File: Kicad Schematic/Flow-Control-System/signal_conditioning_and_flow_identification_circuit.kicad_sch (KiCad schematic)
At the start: 22 parts, among them J13 +5V, J14 GND, U6 NE555P, U7 4093, U8 74HC74, U9 4093

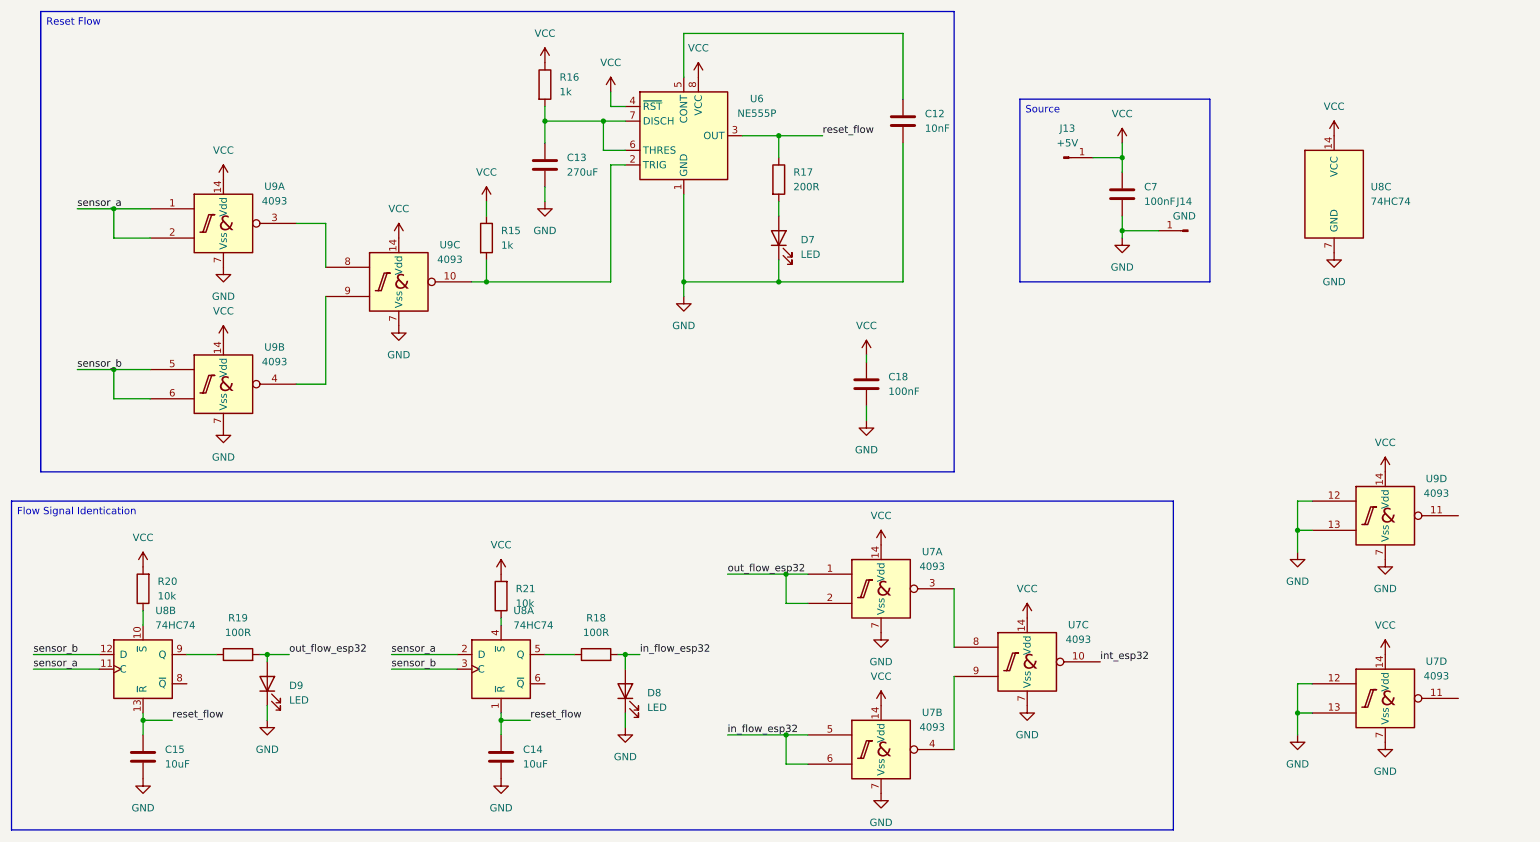
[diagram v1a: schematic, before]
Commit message: - modificação no circuito de reset do 'signal conditioning and flow identification', removido o resistor de pull-up e colocado duas NAND, uma na entrada do trigger e uma na saída, assim, o OUT do 555 só é ativado quando ocorrer um sinal em A ou B, respeitando o timeout calculado previamente - Feito correção na lista de componentes no README.md
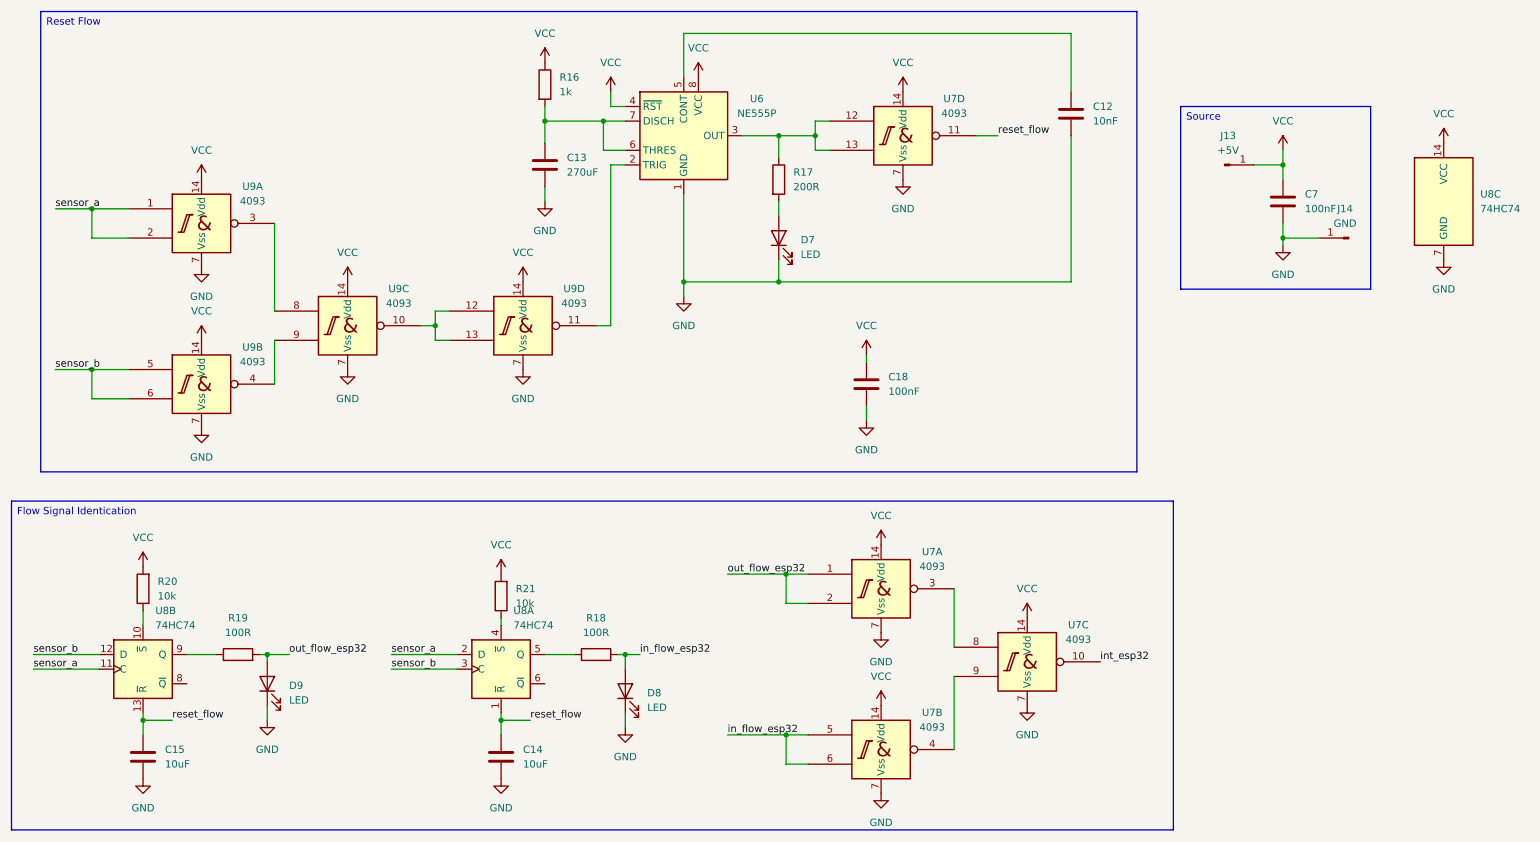
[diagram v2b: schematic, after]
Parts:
- removed R15: 1k, symbol Device:R
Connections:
- net GND: no longer U7.12, U7.13, U9.12, U9.13
- net reset_flow: now also U7.11; no longer R17.1, U6.3 (OUT)
- net at U6.2 (TRIG): now also U9.11; no longer U9.10
- new net: R17.1, U6.3 (OUT), U7.12, U7.13
- new net: U9.10, U9.12, U9.13
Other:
- moved on the sheet: C12, C7, J13, J14, U7D, U8C, U9A, U9B, U9C, U9D

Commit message: - removido a inversora NOT da saída do 555, revertendo o equivoco do projeto - foi substituido os resistores de pull-down R23 e R22 de 1k para 10k
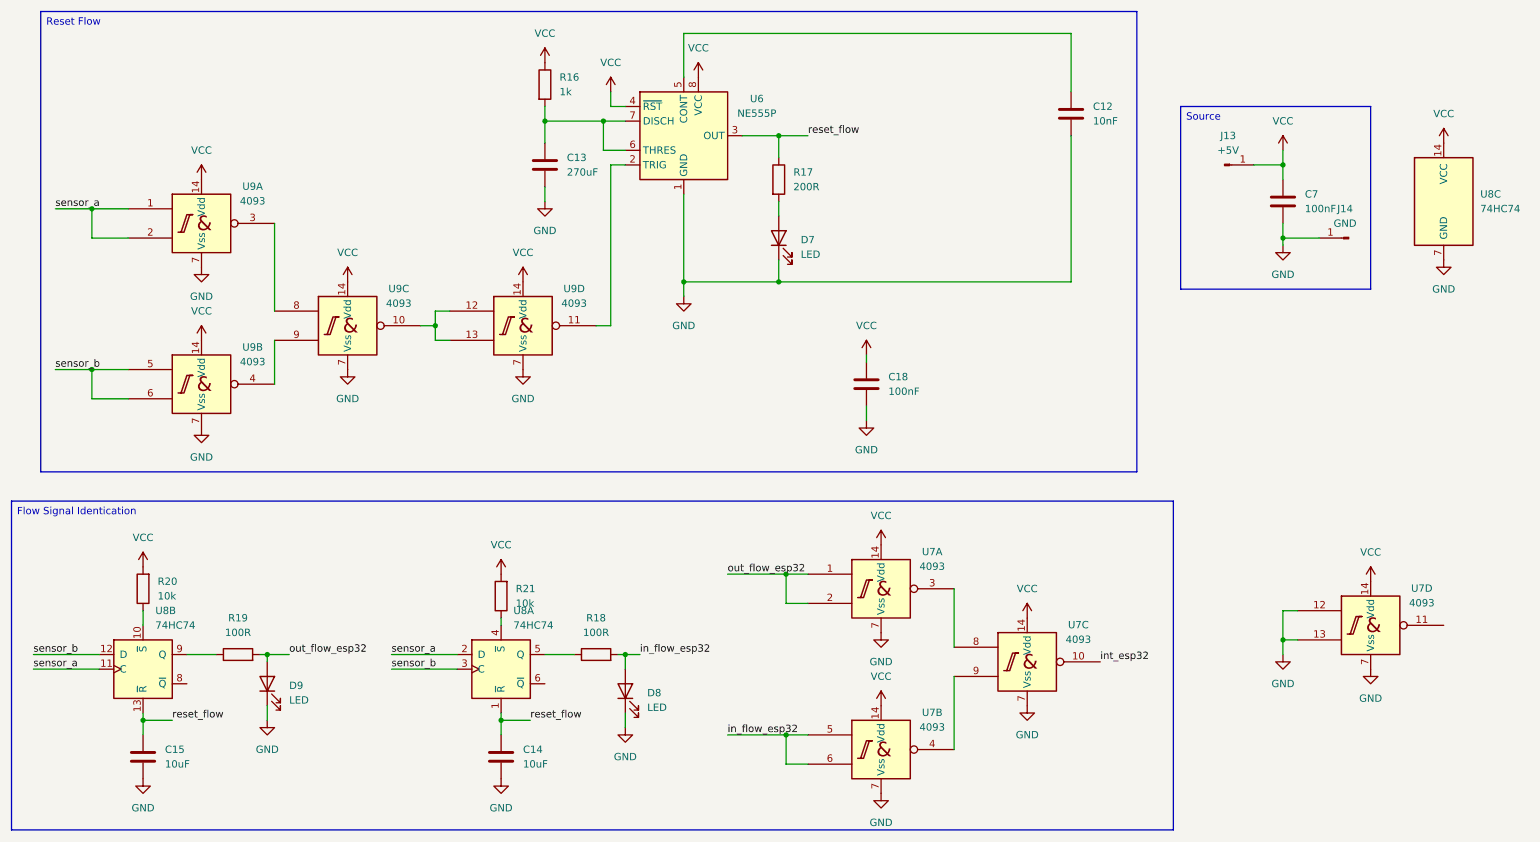
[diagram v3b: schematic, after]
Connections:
- net GND: now also U7.12, U7.13
- net reset_flow: now also R17.1, U6.3 (OUT); no longer U7.11
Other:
- moved on the sheet: U7D

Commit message: - ajuste no circuito, removido dois capacitores de 10uF e adicionado apenas um no circuito de condicionamento de sinal - ajuste na lista de componentes do readme.md
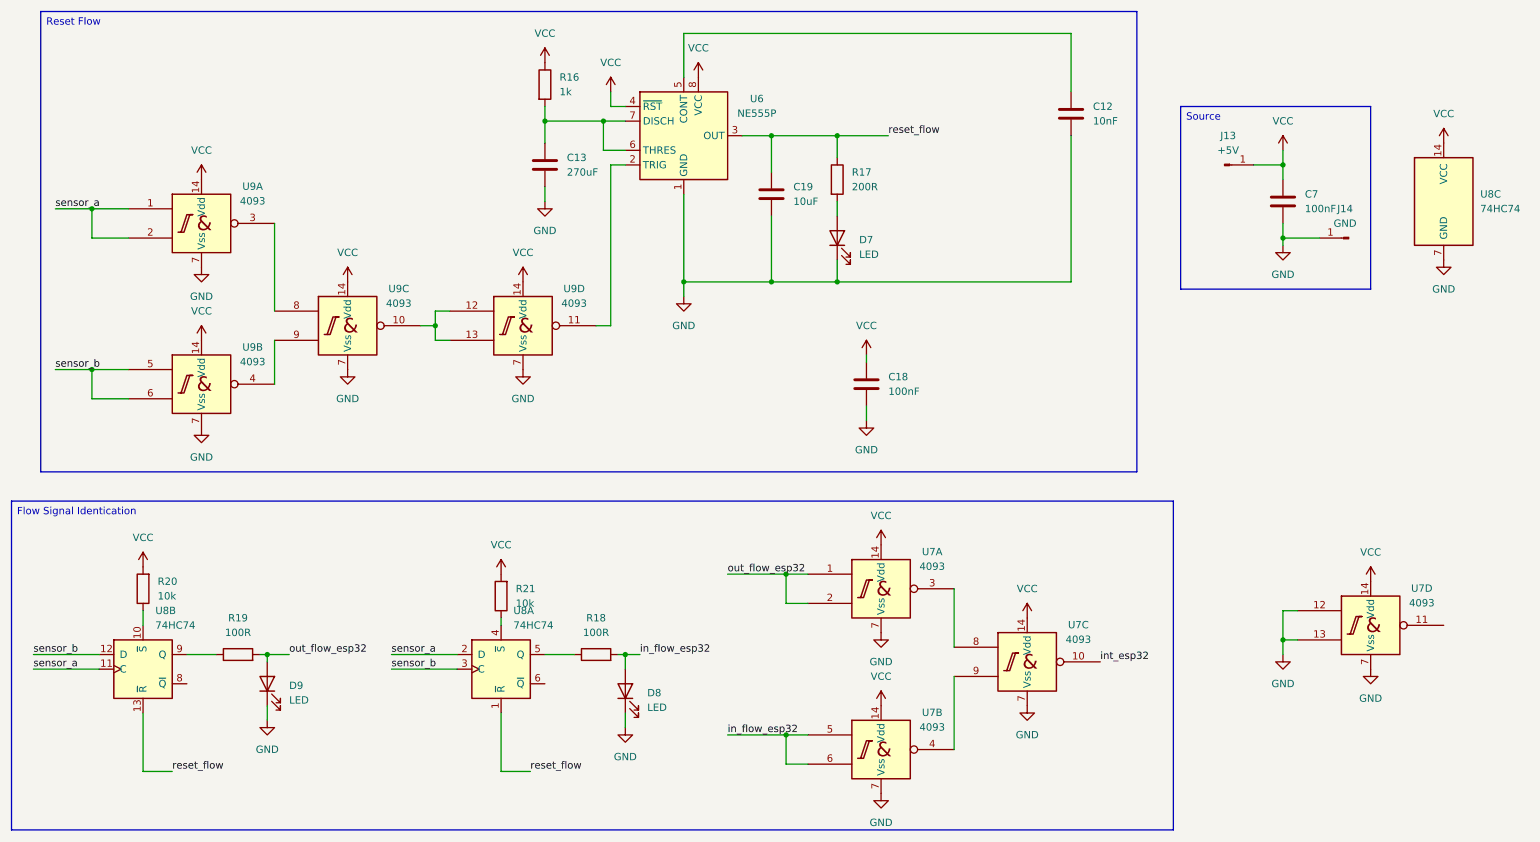
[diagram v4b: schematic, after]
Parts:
- removed C14, C15: 10uF, symbol Device:C
- added C19: 10uF, symbol Device:C
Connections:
- net GND: now also C19.2
- net reset_flow: now also C19.1
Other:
- moved on the sheet: D7, R17
